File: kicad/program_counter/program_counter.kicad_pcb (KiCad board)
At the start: 4 copper layers, 175.3 x 72.4 mm, 109 parts, among them J1 DB37_Male, U1 SN74ALVC00, U10 SN74ALVC00, U11 SN74ALVC00, U12 SN74ALVC00, U13 SN74ALVC00, U14 SN74ALVC00, U15 SN74ALVC00, U16 SN74ALVC00, U17 SN74ALVC00, U18 SN74ALVC00, U19 SN74ALVC00, U2 SN74ALVC00, U20 SN74ALVC00, U21 SN74ALVC00, U22 SN74ALVC00, U23 SN74ALVC00, U24 SN74ALVC00, U25 SN74ALVC00, U26 SN74ALVC00, U27 SN74ALVC00, U28 SN74ALVC00, U29 SN74ALVC00, U3 SN74ALVC00, U30 SN74ALVC00, U31 SN74ALVC00, U32 SN74ALVC00, U33 SN74ALVC00, U34 SN74ALVC00, U35 SN74ALVC00, U36 SN74ALVC00, U37 SN74ALVC00, U38 SN74ALVC00, U39 SN74ALVC00, U4 SN74ALVC00, U40 SN74ALVC00, U41 SN74ALVC00, U42 SN74ALVC00, U43 SN74ALVC00, U44 SN74ALVC00, U45 SN74ALVC00, U46 SN74ALVC00, U47 SN74ALVC00, U48 SN74ALVC00, U49 SN74ALVC00, U5 SN74ALVC00, U50 SN74ALVC00, U51 SN74ALVC00, U52 SN74ALVC00, U53 SN74ALVC00, U54 SN74ALVC00, U55 SN74ALVC00, U56 SN74ALVC00, U57 SN74ALVC00, U58 SN74ALVC00, U59 SN74ALVC00, U6 SN74ALVC00, U60 SN74ALVC00, U61 SN74ALVC00, U62 SN74ALVC00, U63 SN74ALVC00, U64 SN74ALVC00, U65 SN74ALVC00, U66 SN74ALVC00, U67 SN74ALVC00, U68 SN74ALVC00, U69 SN74ALVC00, U7 SN74ALVC00, U70 SN74ALVC00, U71 SN74ALVC00, U72 SN74ALVC00, U73 SN74ALVC00, U74 SN74ALVC00, U75 SN74ALVC00, U76 SN74ALVC00, U8 SN74ALVC00, U9 SN74ALVC00

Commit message: Small routing mods
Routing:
- net clk: track 207.4 -> 204.2 mm, vias 16 -> 17
- net reset: track 191.1 -> 191.7 mm

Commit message: ALU schematic, layout, routing complete. Associated motherboardmod. Also added Load LED to register and program counter boards.
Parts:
- added D16: LED, LED_THT:LED_D5.0mm, F.Cu at (228.6, 73.7)
- added R16: R, Resistor_SMD:R_1206_3216Metric, F.Cu at (224.2, 74.9)
- moved C1 40.6 mm to (231.8, 116.8), turned to 180 degrees
- moved C2 26.7 mm to (233.0, 109.2)
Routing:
- net load: track 204.1 -> 234.7 mm
- net Net-(D16-Pad1): track 0.00 -> 4.50 mm
- net not_load: track 175.2 -> 171.6 mm
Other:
- board text added: "1"
- board text added: "10"
- board text added: "13"
- board text added: "2"
- board text added: "5"
- board text added: "6"
- board text added: "9"
- board text added: "load"

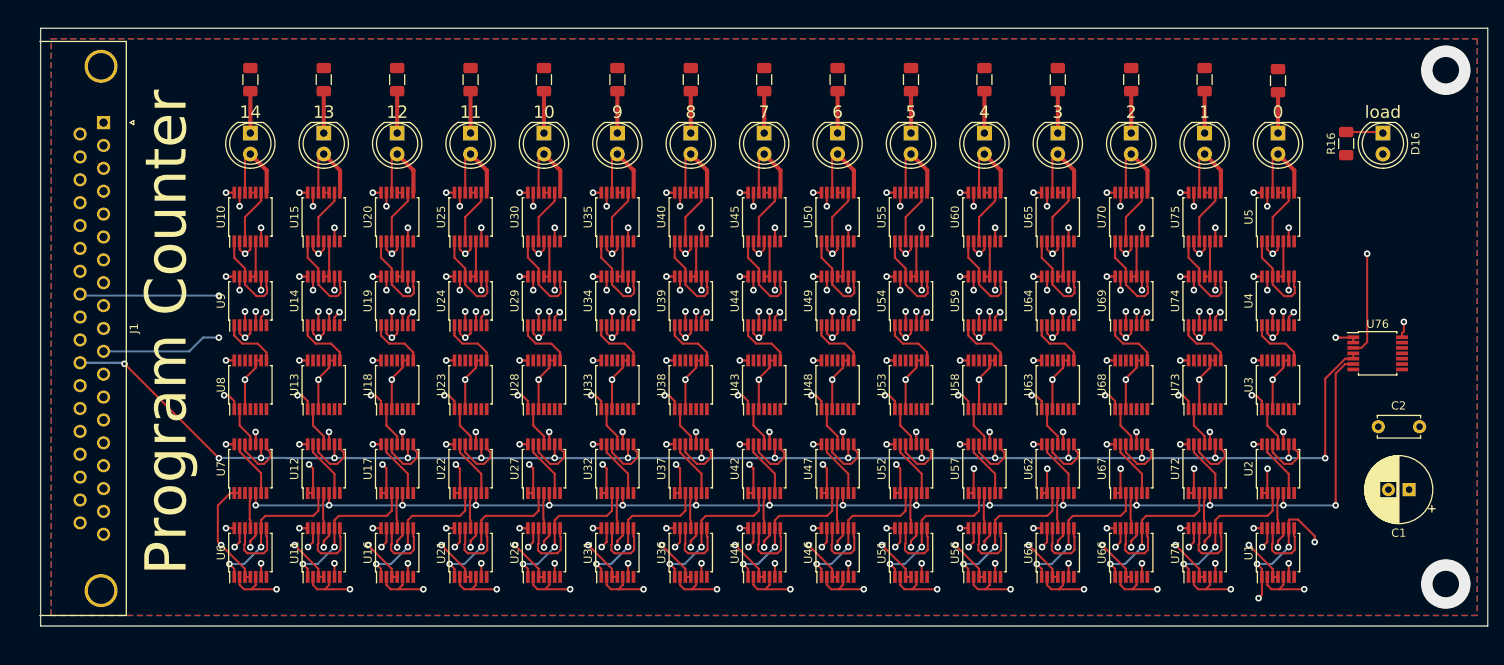
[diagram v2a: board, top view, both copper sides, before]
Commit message: Readme updates (#6)
* Readme intro section

* Board revisions for manufacturing, add digikey PNs to all, added logo.
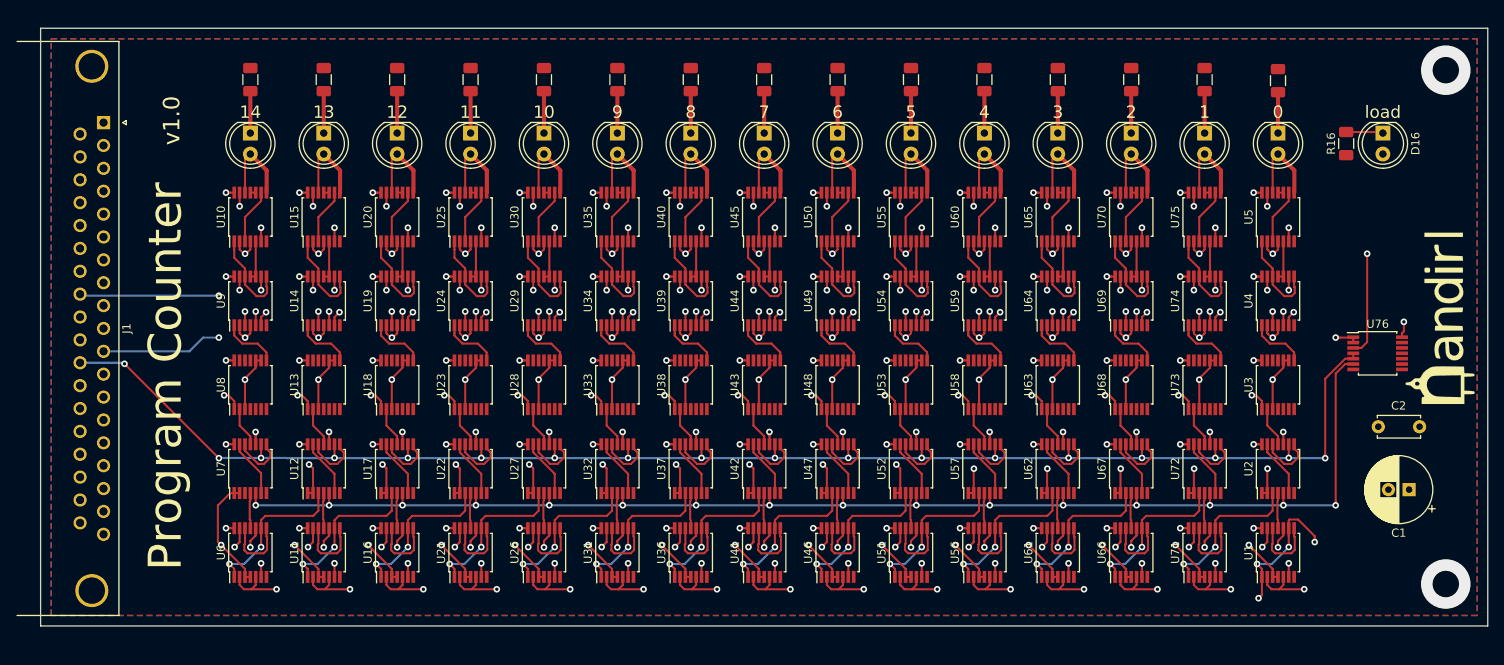
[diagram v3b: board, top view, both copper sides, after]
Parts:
- added G***: LOGO, nandirl logo:logo_sm, F.Cu at (235.6, 95.9)
- J1: footprint Connector_Dsub:DSUB-37_Male_Horizontal_P2.77x2.84mm_EdgePinOffset4.94mm_Housed_MountingHolesOffset7.48mm -> Connector_Dsub:DSUB-37_Male_Horizontal_P2.77x2.84mm_EdgePinOffset7.70mm_Housed_MountingHolesOffset9.12mm
- R1, R10, R11, R12, R13, R14, R15, R16, R2, R3, R4, R5, R6, R7, R8, R9: value R -> 1K
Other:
- board text added: "v1.0"
